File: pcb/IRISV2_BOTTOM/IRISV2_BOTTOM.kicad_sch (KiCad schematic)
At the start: 34 parts, among them J1 Screw_Terminal_01x02, U1 TPS613222ADBV, U2 INA237, U3 MP4323GDE-Z

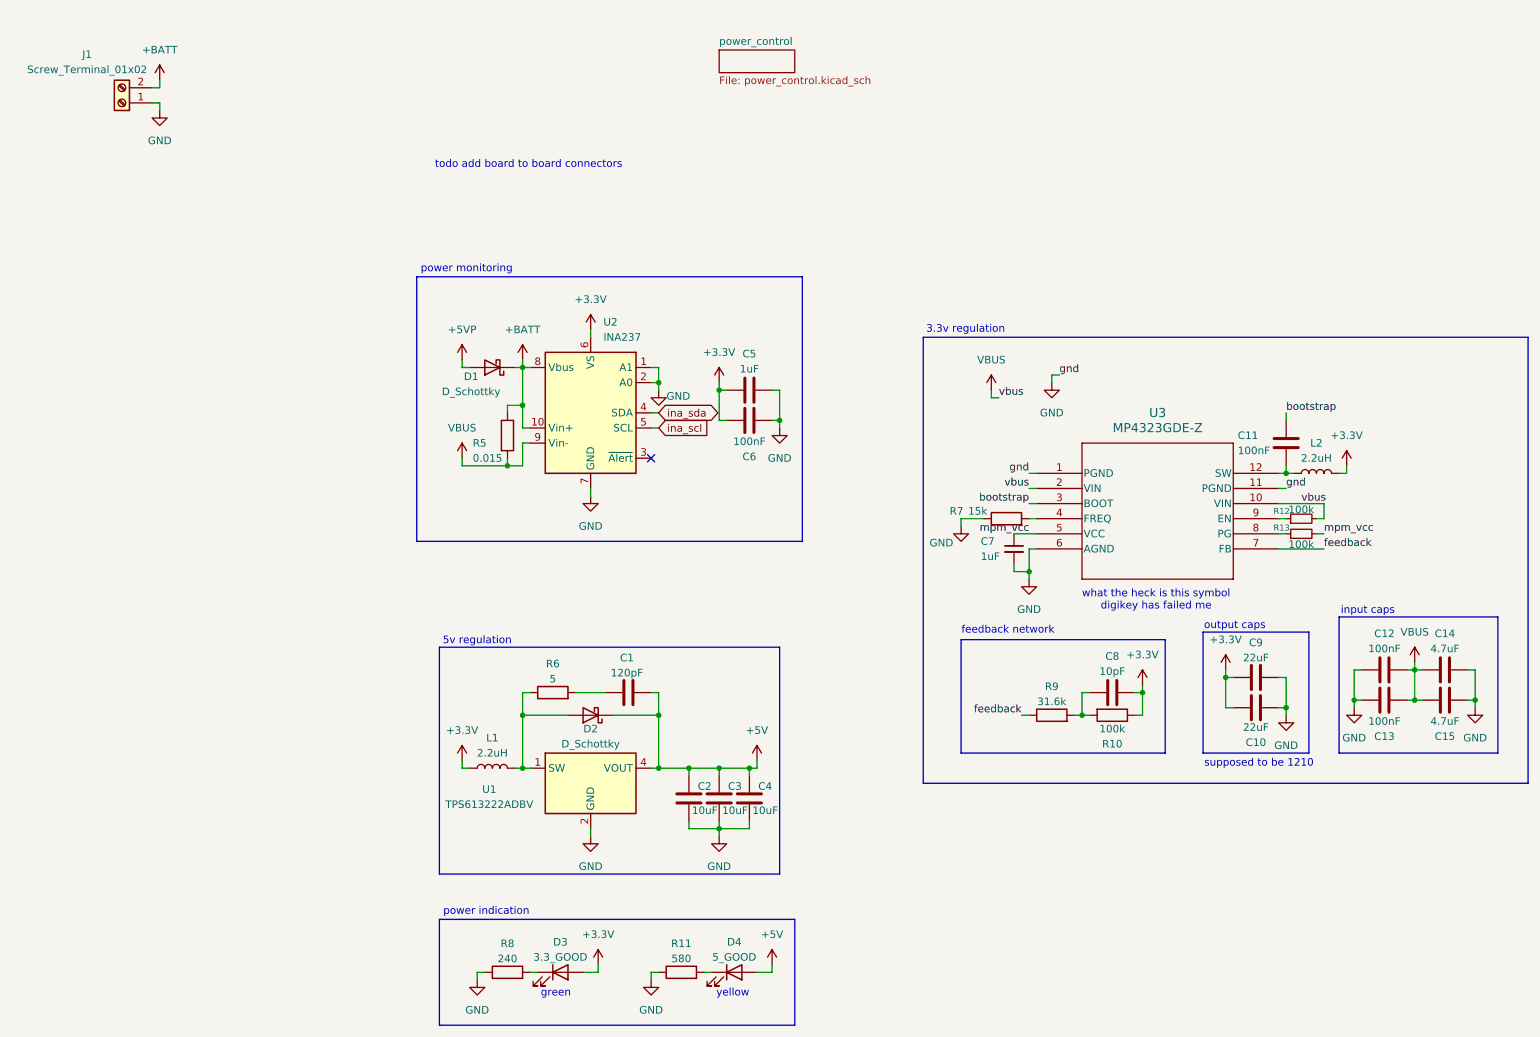
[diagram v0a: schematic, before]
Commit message: bottom pcb now mostly done, connectors selected - now need to finish integrating the connectors and other small tweaks to bottom routing
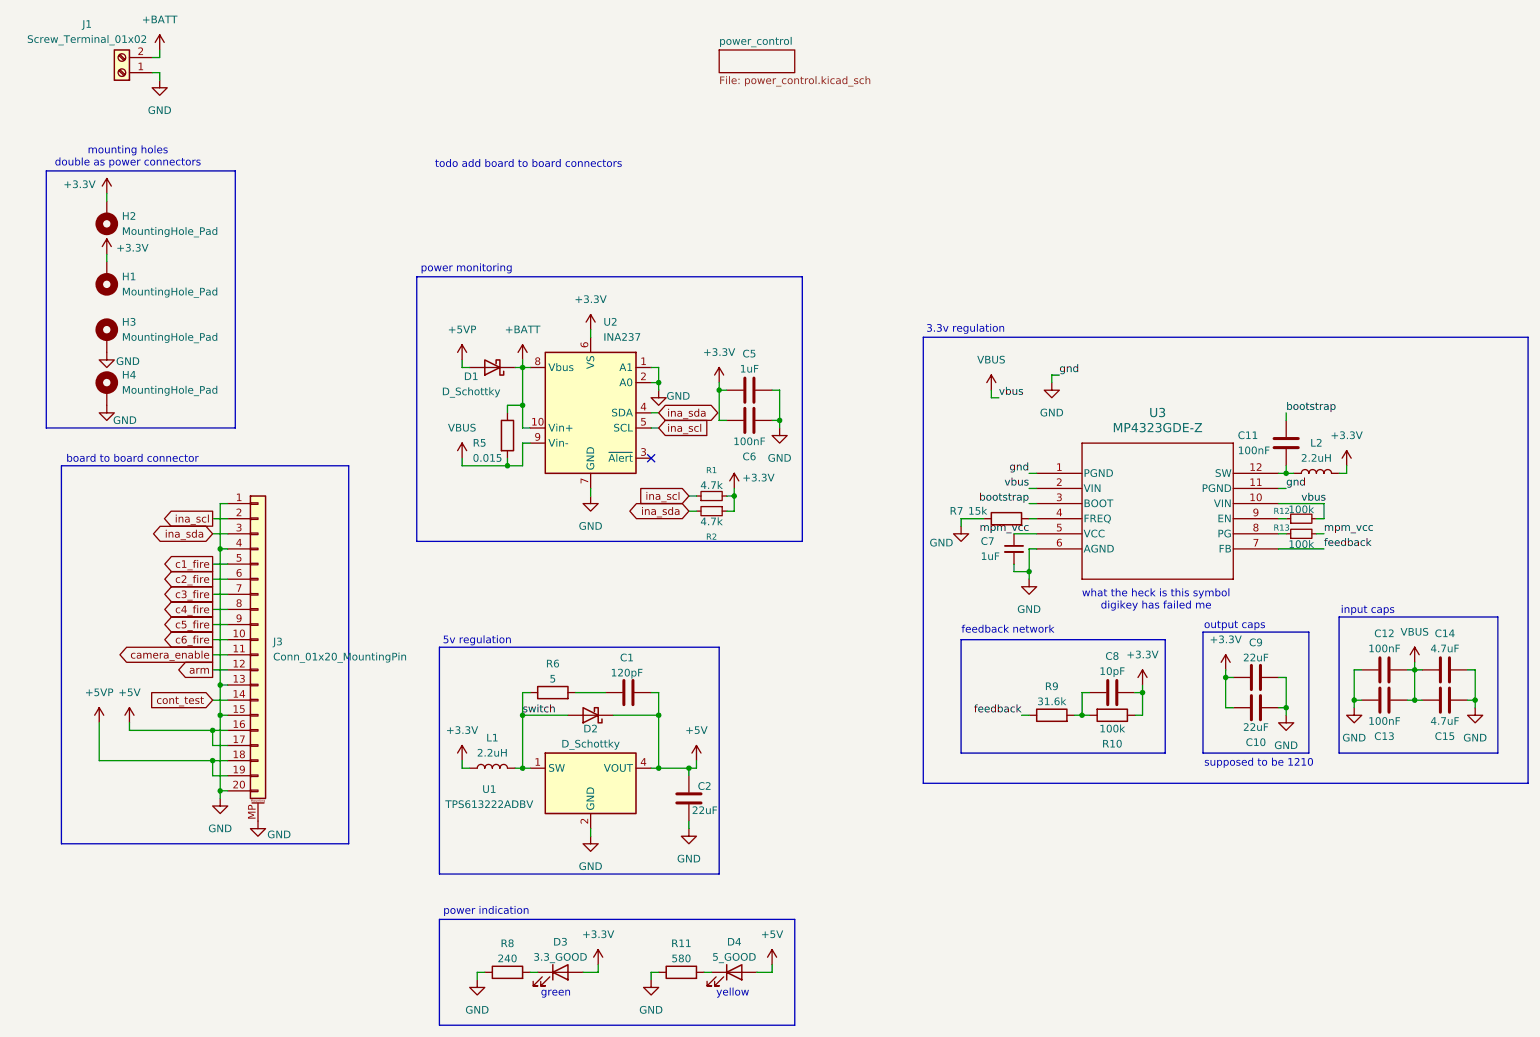
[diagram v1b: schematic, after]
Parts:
- removed C3, C4: 10uF, Capacitor_SMD:C_1206_3216Metric, symbol Device:C
- added H1, H2, H3, H4: MountingHole_Pad, MountingHole:MountingHole_3.2mm_M3_ISO7380_Pad_TopBottom, symbol Mechanical:MountingHole_Pad
- added J3: Conn_01x20_MountingPin, FFC3B07-20-T:FFC3B07-20-T, symbol Connector_Generic_MountingPin:Conn_01x20_MountingPin
- added R1, R2: 4.7k, Resistor_SMD:R_0402_1005Metric, symbol Device:R_Small
- C2: value 10uF -> 22uF
- C8: footprint Capacitor_SMD:C_0603_1608Metric -> Capacitor_SMD:C_0402_1005Metric
- D1, D2: footprint (none) -> SK34SMA-3G:DIOM5027X240N
- J1: footprint TerminalBlock_MetzConnect:TerminalBlock_MetzConnect_Type059_RT06302HBWC_1x02_P3.50mm_Horizontal -> kf350-2p:kf350-2p
- R10, R9: footprint Resistor_SMD:R_0603_1608Metric -> Resistor_SMD:R_0402_1005Metric
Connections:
- net +3.3V: now also H1.1, H2.1, R1.2, R2.1
- net +5V: now also J3.16 (Pin_16), J3.17 (Pin_17)
- net +5VP: now also J3.18 (Pin_18), J3.19 (Pin_19)
- net GND: now also H3.1, H4.1, J3.1 (Pin_1), J3.13 (Pin_13), J3.15 (Pin_15), J3.20 (Pin_20), J3.4 (Pin_4), J3.MP (MountPin)
- net ina_scl: now also J3.2 (Pin_2), R1.1
- net ina_sda: now also J3.3 (Pin_3), R2.2
- net switch: now reaches D2.2 (A), L1.2, R6.1, U1.1 (SW)
- new net arm: J3.12 (Pin_12)
- new net c1_fire: J3.5 (Pin_5)
- new net c2_fire: J3.6 (Pin_6)
- new net c3_fire: J3.7 (Pin_7)
- new net c4_fire: J3.8 (Pin_8)
- new net c5_fire: J3.9 (Pin_9)
- new net c6_fire: J3.10 (Pin_10)
- new net camera_enable: J3.11 (Pin_11)
- new net cont_test: J3.14 (Pin_14)
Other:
- note added: "board to board connector"
- note added: "mounting holes double as power connectors"
- moved on the sheet: J1

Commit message: bottom board design done, need to polish it
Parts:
- added BZ1: Buzzer, CMT-8504-03-SMT:CMT850403SMTTR, symbol Device:Buzzer
- added Q17: BC846, Package_TO_SOT_SMD:SOT-23-3, symbol Simulation_SPICE:NPN
- added R3: 1k, Resistor_SMD:R_0402_1005Metric, symbol Device:R
- added R4: 10k, Resistor_SMD:R_0402_1005Metric, symbol Device:R
- D3, D4: footprint (none) -> LED_SMD:LED_0805_2012Metric
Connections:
- net +3.3V: now also BZ1.1 (+), R4.1
- net GND: now also Q17.3 (E); no longer J3.20 (Pin_20)
- new net: BZ1.2 (-), Q17.1 (C)
- new net: Q17.2 (B), R3.2, R4.2
- new net buzzer: J3.20 (Pin_20), R3.1
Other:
- note added: "buzzer"
